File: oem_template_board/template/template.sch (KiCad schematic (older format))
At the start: 29 parts, among them J1 CONN_02X03, U1 MCP2561-E_SN, U101 TPS560430YF, U2 ATMEGA16M1, Y1 Crystal_SMD

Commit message: updated template project, removed rescue library, replaced rescued components with formula components, changed VCC to +5V, added note not to move programming connection, removed unnecessary power flags
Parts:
- C1, C101, C103, C2: symbol template-rescue:C_0.1uF-formula -> formula:C_0.1uF
- C102: symbol template-rescue:C_2.2uF-formula -> formula:C_2.2uF
- C3: symbol template-rescue:C_100pF-formula -> formula:C_100pF
- C4, C5: symbol template-rescue:C_30pF-formula -> formula:C_30pF
- COUT101: symbol template-rescue:C_22uF-formula -> formula:C_22uF
- COUT102: symbol template-rescue:C_33uF-formula -> formula:C_33uF
- COUT103: symbol template-rescue:C_47uF-formula -> formula:C_47uF
- D101: symbol template-rescue:D_Zener_18V-formula -> formula:D_Zener_18V
- D102, D103: symbol template-rescue:LED_0805-formula -> formula:LED_0805
- F101: symbol template-rescue:F_500mA_16V-formula -> formula:F_500mA_16V
- J1: symbol template-rescue:CONN_02X03-formula -> formula:CONN_02X03
- L101: symbol template-rescue:L_100uH-formula -> formula:L_100uH
- R1: symbol template-rescue:R_100-formula -> formula:R_100
- R102: symbol template-rescue:R_25K-formula -> formula:R_25K
- R103: symbol template-rescue:R_100K-formula -> formula:R_100K
- R104: symbol template-rescue:R_0_2512-formula -> formula:R_0_2512
- R105: symbol template-rescue:R_200-formula -> formula:R_200
- R3: symbol template-rescue:R_10K-formula -> formula:R_10K
- U1: symbol template-rescue:MCP2561-E_SN-formula -> formula:MCP2561-E_SN
- U101: symbol template-rescue:TPS560430YF-formula -> formula:TPS560430YF
- U2: symbol template-rescue:ATMEGA16M1-formula -> formula:ATMEGA16M1
- Y1: symbol template-rescue:Crystal_SMD-formula -> formula:Crystal_SMD
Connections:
- net VCC renamed +5V
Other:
- note added: "MOSI, MISO, and SCK must\nstay connected to the _A pins\nfor programming."
- note removed: "5V"
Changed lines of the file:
@@
 $EndComp
 $Comp
-L template-rescue:C_2.2uF-formula C102
+L formula:C_2.2uF C102
 U 1 1 5BEE2647
-P 2400 8950
-F 0 "C102" H 2450 8800 50  0000 L CNN
-F 1 "C_2.2uF" H 2280 9200 50  0000 L CNN
-F 2 "footprints:C_0603_1608Metric" H 2438 8800 50  0001 C CNN
-F 3 "http://www.yageo.com/documents/recent/UPY-GPHC_X5R_4V-to-50V_25.pdf" H 2425 9050 50  0001 C CNN
-F 4 "DK" H 2400 8950 60  0001 C CNN "MFN"
-F 5 "311-1451-1-ND" H 2400 8950 60  0001 C CNN "MPN"
-F 6 "https://www.digikey.com/product-detail/en/yageo/CC0603KRX5R6BB225/311-1451-1-ND/2833757" H 2825 9450 60  0001 C CNN "PurchasingLink"
-	1    2400 8950
-	1    0    0    -1
-$EndComp
-$Comp
-L template-rescue:C_0.1uF-formula C101
+P 2400 9000
+F 0 "C102" H 2450 8850 50  0000 L CNN
+F 1 "C_2.2uF" H 2280 9250 50  0000 L CNN
+F 2 "footprints:C_0603_1608Metric" H 2438 8850 50  0001 C CNN
+F 3 "http://www.yageo.com/documents/recent/UPY-GPHC_X5R_4V-to-50V_25.pdf" H 2425 9100 50  0001 C CNN
+F 4 "DK" H 2400 9000 60  0001 C CNN "MFN"
+F 5 "311-1451-1-ND" H 2400 9000 60  0001 C CNN "MPN"
+F 6 "https://www.digikey.com/product-detail/en/yageo/CC0603KRX5R6BB225/311-1451-1-ND/2833757" H 2825 9500 60  0001 C CNN "PurchasingLink"
+	1    2400 9000
+	1    0    0    -1
+$EndComp
+$Comp
+L formula:C_0.1uF C101
 U 1 1 5BEE2923
 P 2100 8950
@@
 $EndComp
 $Comp
-L template-rescue:R_100K-formula R103
+L formula:R_100K R103
 U 1 1 5BEE2A52
 P 4000 9600
@@
 $EndComp
 $Comp
-L template-rescue:C_0.1uF-formula C103
+L formula:C_0.1uF C103
 U 1 1 5BEE239B
 P 4000 8750
@@
 12V
 $Comp
-L template-rescue:C_22uF-formula COUT101
+L formula:C_22uF COUT101
 U 1 1 5C061BB4
 P 4800 9050
@@
 $EndComp
 $Comp
-L template-rescue:C_47uF-formula COUT103
+L formula:C_47uF COUT103
 U 1 1 5C062E7A
 P 5600 9050
@@
 $EndComp
 $Comp
-L template-rescue:C_33uF-formula COUT102
+L formula:C_33uF COUT102
 U 1 1 5C08921B
 P 5200 9050
@@
 $EndComp
 $Comp
-L template-rescue:R_25K-formula R102
+L formula:R_25K R102
 U 1 1 5C0B315C
 P 3500 9600
@@
 $EndComp
 $Comp
-L template-rescue:F_500mA_16V-formula F101
+L formula:F_500mA_16V F101
 U 1 1 5C0BFA29
 P 1050 8800
@@
 $EndComp
 $Comp
-L template-rescue:R_0_2512-formula R104
+L formula:R_0_2512 R104
 U 1 1 5C0C29A9
 P 6150 8900
@@
 $EndComp
 $Comp
-L template-rescue:LED_0805-formula D103
+L formula:LED_0805 D103
 U 1 1 5C0C344A
 P 6550 9750
@@
 $EndComp
 $Comp
-L template-rescue:R_200-formula R105
+L formula:R_200 R105
 U 1 1 5C0C44F9
 P 6550 9150
@@
 $EndComp
 $Comp
-L template-rescue:D_Zener_18V-formula D101
+L formula:D_Zener_18V D101
 U 1 1 5C623D49
 P 1300 9100
@@
 12V
 $Comp
-L template-rescue:LED_0805-formula D102
+L formula:LED_0805 D102
 U 1 1 5C754D7D
 P 1700 9350
@@
 Text Notes 5950 8800 0    50   ~ 0
 VCC Jumper\n
-$Comp
-L power:VCC #PWR0112
-U 1 1 5C74E72F
-P 6550 8750
-F 0 "#PWR0112" H 6550 8600 50  0001 C CNN
-F 1 "VCC" H 6567 8923 50  0000 C CNN
-F 2 "" H 6550 8750 50  0001 C CNN
-F 3 "" H 6550 8750 50  0001 C CNN
-	1    6550 8750
-	1    0    0    -1
-$EndComp
-Text Notes 6650 8700 0    50   ~ 0
-5V
 Text Notes 6400 10000 1    50   ~ 0
 5V Indicator
 $Comp
-L template-rescue:ATMEGA16M1-formula U2
+L formula:ATMEGA16M1 U2
 U 1 1 5D58A7A6
 P 2550 2700
@@
 RESET
 $Comp
-L template-rescue:R_100-formula R1
+L formula:R_100 R1
 U 1 1 5D58E16F
 P 1150 1150
@@
 $EndComp
 $Comp
-L template-rescue:C_100pF-formula C3
+L formula:C_100pF C3
 U 1 1 5D58E505
 P 1150 1450
@@
 $EndComp
 $Comp
-L template-rescue:Crystal_SMD-formula Y1
+L formula:Crystal_SMD Y1
 U 1 1 5D5EB332
 P 4100 4100
@@
 $EndComp
 $Comp
-L template-rescue:C_30pF-formula C4
+L formula:C_30pF C4
 U 1 1 5D5EB5B2
 P 3900 4350
@@
 $EndComp
 $Comp
-L template-rescue:C_30pF-formula C5
+L formula:C_30pF C5
 U 1 1 5D5EB694
 P 4300 4350
@@
 $EndComp
 $Comp
-L template-rescue:R_10K-formula R3
+L formula:R_10K R3
 U 1 1 5D5EB7F3
 P 4150 3500
@@
 $EndComp
 $Comp
-L power:VCC #PWR08
-U 1 1 5D5F7547
-P 4450 3350
-F 0 "#PWR08" H 4450 3200 50  0001 C CNN
-F 1 "VCC" H 4560 3410 50  0000 C CNN
-F 2 "" H 4450 3350 50  0001 C CNN
-F 3 "" H 4450 3350 50  0001 C CNN
-	1    4450 3350
-	1    0    0    -1
-$EndComp
-$Comp
 L power:GND #PWR011
 U 1 1 5D5F86E8
@@
 $EndComp
 $Comp
-L template-rescue:MCP2561-E_SN-formula U1
+L formula:MCP2561-E_SN U1
 U 1 1 5D5FAEDE
 P 14800 2050
@@
 $EndComp
 $Comp
-L template-rescue:C_0.1uF-formula C1
+L formula:C_0.1uF C1
 U 1 1 5D5FB603
 P 14650 1450
@@
 $EndComp
 NoConn ~ 15300 2050
-$Comp
-L power:VCC #PWR01
-U 1 1 5D602F58
-P 14800 1300
-F 0 "#PWR01" H 14800 1150 50  0001 C CNN
-F 1 "VCC" H 14817 1473 50  0000 C CNN
-F 2 "" H 14800 1300 50  0001 C CNN
-F 3 "" H 14800 1300 50  0001 C CNN
-	1    14800 1300
-	1    0    0    -1
-$EndComp
 $Comp
 L power:GND #PWR02
@@
 $EndComp
 $Comp
-L power:VCC #PWR016
-U 1 1 5D6181B6
-P 14950 8600
-F 0 "#PWR016" H 14950 8450 50  0001 C CNN
-F 1 "VCC" H 14968 8773 50  0000 C CNN
-F 2 "" H 14950 8600 50  0001 C CNN
-F 3 "" H 14950 8600 50  0001 C CNN
-	1    14950 8600
-	-1   0    0    1
-$EndComp
-Text Label 14250 8600 0    50   ~ 0
-5V
-$Comp
-L power:VCC #PWR015
-U 1 1 5D61D085
-P 14250 8450
-F 0 "#PWR015" H 14250 8300 50  0001 C CNN
-F 1 "VCC" H 14267 8623 50  0000 C CNN
-F 2 "" H 14250 8450 50  0001 C CNN
-F 3 "" H 14250 8450 50  0001 C CNN
-	1    14250 8450
-	1    0    0    -1
-$EndComp
-$Comp
-L power:GND #PWR017
-U 1 1 5D622997
-P 15650 8600
-F 0 "#PWR017" H 15650 8350 50  0001 C CNN
-F 1 "GND" H 15655 8427 50  0000 C CNN
-F 2 "" H 15650 8600 50  0001 C CNN
-F 3 "" H 15650 8600 50  0001 C CNN
-	1    15650 8600
-	1    0    0    -1
-$EndComp
-Text Label 15650 8450 2    50   ~ 0
-GND
-$Comp
-L template-rescue:CONN_02X03-formula J1
+L formula:CONN_02X03 J1
 U 1 1 5D628C9D
 P 14850 3750
@@
 	1    0    0    -1
 $EndComp
-$Comp
-L power:VCC #PWR07
-U 1 1 5D6297EA
-P 15100 3650
-F 0 "#PWR07" H 15100 3500 50  0001 C CNN
-F 1 "VCC" H 15117 3823 50  0000 C CNN
-F 2 "" H 15100 3650 50  0001 C CNN
-F 3 "" H 15100 3650 50  0001 C CNN
-	1    15100 3650
-	1    0    0    -1
-$EndComp
 Text Notes 13850 3400 0    89   ~ 0
 16M1 PROGRAMMING HEADER\n
-$Comp
-L power:VCC #PWR018
-U 1 1 5DB132A0
-P 800 850
-F 0 "#PWR018" H 800 700 50  0001 C CNN
-F 1 "VCC" H 817 1023 50  0000 C CNN
-F 2 "" H 800 850 50  0001 C CNN
-F 3 "" H 800 850 50  0001 C CNN
-	1    800  850
-	1    0    0    -1
-$EndComp
 Wire Wire Line
 	1450 1300 1150 1300
 Connection ~ 1150 1300
 $Comp
-L template-rescue:C_0.1uF-formula C2
+L formula:C_0.1uF C2
 U 1 1 5D58E34B
 P 800 1150
@@
 	15400 2150 15400 2200
 Wire Wire Line
-	14250 8450 14250 8600
-Wire Wire Line
 	14550 8450 14550 8600
 Wire Wire Line
@@
 Wire Wire Line
 	15350 8450 15350 8600
-Wire Wire Line
-	15650 8450 15650 8600
 Wire Wire Line
 	3500 8750 3850 8750
@@
 Connection ~ 2100 8800
 Wire Wire Line
-	2100 8800 2400 8800
-Connection ~ 2400 8800
-Wire Wire Line
-	2400 8800 2650 8800
-Wire Wire Line
 	1700 9100 1700 9200
 Wire Wire Line
@@
 	800  8500 800  8800
 $Comp
-L template-rescue:TPS560430YF-formula U101
+L formula:TPS560430YF U101
 U 1 1 5C75D405
 P 3100 8950
@@
 $EndComp
 $Comp
-L template-rescue:L_100uH-formula L101
+L formula:L_100uH L101
 U 1 1 5F881F17
 P 4400 8900
@@
 Wire Wire Line
 	15600 2200 15750 2200
+Wire Wire Line
+	2100 8800 2400 8800
+$Comp
+L power:+5V #PWR?
+U 1 1 5FD33116
+P 6550 8750
+F 0 "#PWR?" H 6550 8600 50  0001 C CNN
+F 1 "+5V" H 6565 8923 50  0000 C CNN
+F 2 "" H 6550 8750 50  0001 C CNN
+F 3 "" H 6550 8750 50  0001 C CNN
+	1    6550 8750
+	1    0    0    -1
+$EndComp
+$Comp
+L power:+5V #PWR?
+U 1 1 5FD33423
+P 800 850
+F 0 "#PWR?" H 800 700 50  0001 C CNN
+F 1 "+5V" H 815 1023 50  0000 C CNN
+F 2 "" H 800 850 50  0001 C CNN
+F 3 "" H 800 850 50  0001 C CNN
+	1    800  850
+	1    0    0    -1
+$EndComp
+$Comp
+L power:+5V #PWR?
+U 1 1 5FD3B2BE
+P 14800 1300
+F 0 "#PWR?" H 14800 1150 50  0001 C CNN
+F 1 "+5V" H 14815 1473 50  0000 C CNN
+F 2 "" H 14800 1300 50  0001 C CNN
+F 3 "" H 14800 1300 50  0001 C CNN
+	1    14800 1300
+	1    0    0    -1
+$EndComp
+$Comp
+L power:+5V #PWR?
+U 1 1 5FD3C2F8
+P 15100 3650
+F 0 "#PWR?" H 15100 3500 50  0001 C CNN
+F 1 "+5V" H 15115 3823 50  0000 C CNN
+F 2 "" H 15100 3650 50  0001 C CNN
+F 3 "" H 15100 3650 50  0001 C CNN
+	1    15100 3650
+	1    0    0    -1
+$EndComp
+$Comp
+L power:+5V #PWR?
+U 1 1 5FD3CE98
+P 14950 8600
+F 0 "#PWR?" H 14950 8450 50  0001 C CNN
+F 1 "+5V" H 14965 8773 50  0000 C CNN
+F 2 "" H 14950 8600 50  0001 C CNN
+F 3 "" H 14950 8600 50  0001 C CNN
+	1    14950 8600
+	-1   0    0    1
+$EndComp
+Connection ~ 2400 8800
+Wire Wire Line
+	2400 8800 2650 8800
+Text Notes 3900 3050 0    50   ~ 0
+MOSI, MISO, and SCK must\nstay connected to the _A pins\nfor programming.
+$Comp
+L power:+5V #PWR?
+U 1 1 5FD477AE
+P 4450 3350
+F 0 "#PWR?" H 4450 3200 50  0001 C CNN
+F 1 "+5V" H 4465 3523 50  0000 C CNN
+F 2 "" H 4450 3350 50  0001 C CNN
+F 3 "" H 4450 3350 50  0001 C CNN
+	1    4450 3350
+	1    0    0    -1
+$EndComp
 $EndSCHEMATC

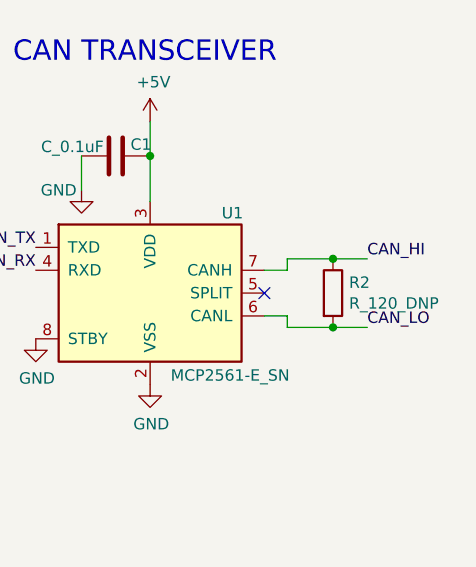
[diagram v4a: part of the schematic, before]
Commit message: changed template CAN net labels to _+ and _- for differential routing, updated template pdf
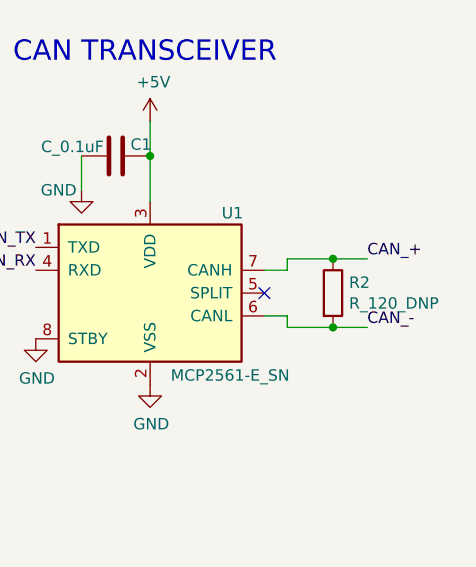
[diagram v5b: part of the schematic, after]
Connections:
- net CAN_HI renamed CAN_+
- net CAN_LO renamed CAN_-
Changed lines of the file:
@@
 CAN_RX
 Text Label 15750 1900 0    50   ~ 0
-CAN_HI
+CAN_+
 Text Label 15750 2200 0    50   ~ 0
-CAN_LO
+CAN_-
 Text Notes 14200 1050 0    89   ~ 0
 CAN TRANSCEIVER\n
